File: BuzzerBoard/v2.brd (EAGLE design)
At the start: 48 x 15 mm, 10 parts, among them J1 p0, U1 LM386MX-1/NOPB

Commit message: starting on v2
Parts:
- removed R1: 23BR100KLFTR, BuzzerLib:SOT_23BR100KLFTR
- removed U$1: SMS-1308MS-2-R, BuzzerLib:SMS-1308MS-2-R
- added C5: GRM188R60J106ME47D, BuzzerLib:0603
- added C6: C2012X5R1A336M125AC, BuzzerLib:0805
- added J2: (no value), SparkFun-Connectors:1X02
- added U2: Value, BuzzerLib:DRC0010J
- added U3: LQM2HPN1R5MG0L, BuzzerLib:1008
- moved R2 19.7 mm to (34.1, 8.19), turned to 180 degrees
- moved C2 19.5 mm to (34.1, 11.7), turned to 270 degrees
- moved C4 17.0 mm to (38.9, 12.7)
- moved C3 11.0 mm to (43.4, 7.49)
- moved C1 11.0 mm to (38.9, 8.48)
- moved U1 11.0 mm to (38.9, 4.08)
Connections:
- removed net IN+: R1.2, U1.3
- new net 3V_REG: C6.1, U1.6, U2.1, U2.10
- new net N$6: U2.2, U3.2
- new net N$7: U2.4, U3.1
- net +: now also J2.1; no longer U$1.+
- net 3.3V: now also C5.1, U2.5, U2.6, U2.7, U2.8; no longer U1.6
- net GND: now also C5.2, C6.2, J2.2, U2.11, U2.3, U2.9; no longer R1.1, U$1.-
- net P0: now also U1.3; no longer R1.3
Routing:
- net GND: track 21.3 -> 0.00 mm, vias 9 -> 0
- net +: track 13.9 -> 0.00 mm
- net VOUT: track 32.7 -> 21.1 mm, vias 4 -> 0
- net P0: track 10.6 -> 0.00 mm
- net IN+: track 8.09 -> 0.00 mm
- net GAIN: track 4.61 -> 0.00 mm
- net BYPASS: track 4.51 -> 0.00 mm
- net N$2: track 4.42 -> 0.00 mm
- net N$1: track 1.92 -> 0.00 mm

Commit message: progress on the v2 board
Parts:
- removed U2: Value, BuzzerLib:DRC0010J
- removed U3: LQM2HPN1R5MG0L, BuzzerLib:1008
- added C7: 100nf, Seeed-Capacitor:C0603
- added J3: inv, SparkFun-Connectors:1X02
- C5: value GRM188R60J106ME47D -> 100pf; device BuzzerLib:0603 -> Seeed-Capacitor:C0603
- C6: value C2012X5R1A336M125AC -> 100nf; device BuzzerLib:0805 -> Seeed-Capacitor:C0603
- J1: value p0 -> input
- J2: value (none) -> speaker
- moved U$2 21.0 mm to (24.0, 3.00)
- moved R2 20.3 mm to (13.9, 9.47), turned to 270 degrees
- moved C2 20.2 mm to (13.9, 11.4), turned to 180 degrees
- moved J2 19.9 mm to (26.6, 10.7)
- moved C4 18.7 mm to (20.3, 11.7)
- moved U1 14.8 mm to (24.2, 3.38)
- moved C1 14.7 mm to (24.1, 7.28)
- moved C3 14.4 mm to (29.2, 4.84)
- moved C5 14.0 mm to (19.4, 5.50), turned to 180 degrees
- moved C6 6.39 mm to (15.7, 5.50), turned to 0 degrees
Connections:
- removed net 3V_REG: C6.1, U1.6, U2.1, U2.10
- removed net N$6: U2.2, U3.2
- removed net N$7: U2.4, U3.1
- new net IN-: J3.2, U1.2
- new net N$3: C5.1, J3.1
- net +: now also J2.2; no longer J2.1
- net 3.3V: now also C6.2, U1.6; no longer C5.1, U2.5, U2.6, U2.7, U2.8
- net GND: now also C6.1, C7.1, J2.1; no longer C6.2, J2.2, U1.2, U2.11, U2.3, U2.9
- net P0: now also C7.2
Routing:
- net VOUT: track 21.1 -> 0.00 mm
- net P0: track 0.00 -> 6.10 mm
- net IN-: track 0.00 -> 4.89 mm
- net N$3: track 0.00 -> 4.78 mm
- net +: track 0.00 -> 4.68 mm
- net GAIN: track 0.00 -> 3.41 mm
- net N$2: track 0.00 -> 3.33 mm
- net 3.3V: track 0.00 -> 3.20 mm
- net N$1: track 0.00 -> 1.99 mm
- added copper zone on layer 16, net 3.3V
- added copper zone on layer 1, net GND
- removed copper zone on layer 1, net 3.3V
- removed copper zone on layer 16, net GND
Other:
- board text added: "+"
- board text added: "3.3v"
- board text added: "GND"
- board text added: "Moto:Bit Speaker v1.0 32bits.io"
- board text added: "P0"
- board text added: "bee-boo-boop-beep"
- board text removed: "Moto:Bit Speaker v1.0 | 32bits.io"

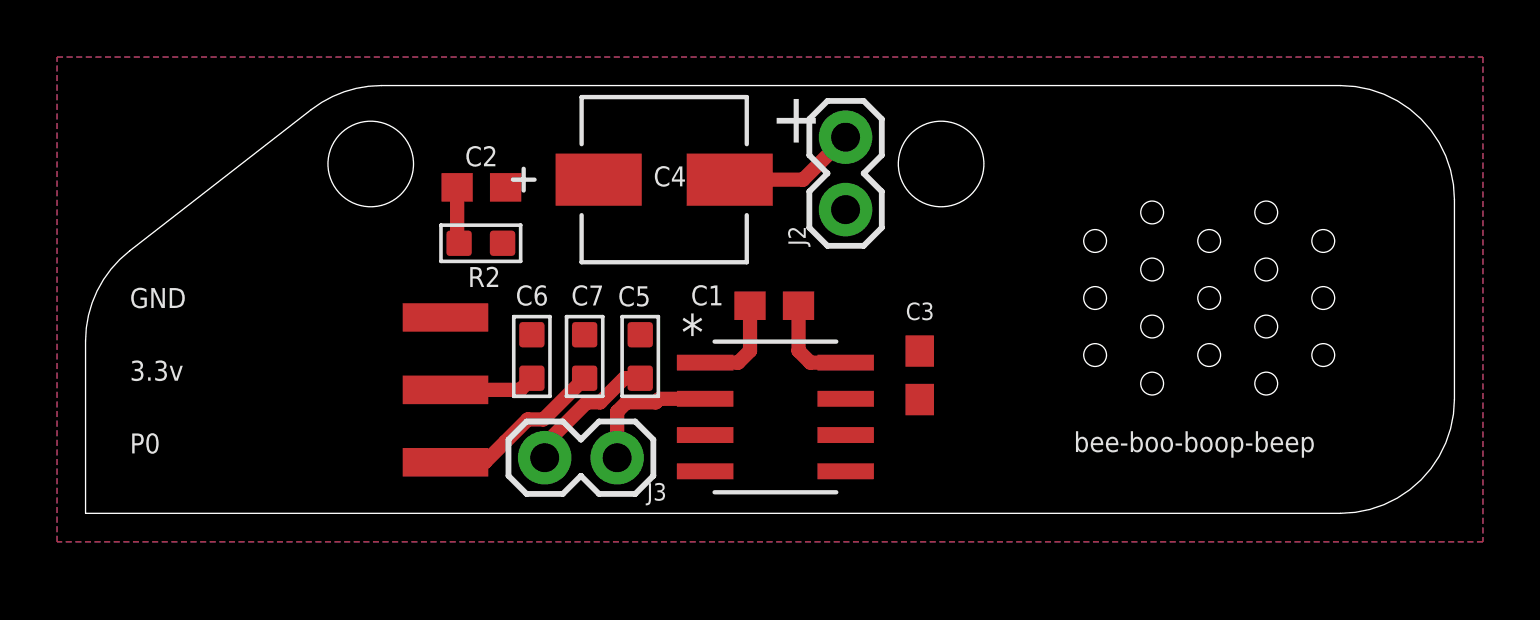
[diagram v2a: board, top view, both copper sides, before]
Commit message: Switching to LM48310 on the v2 board.
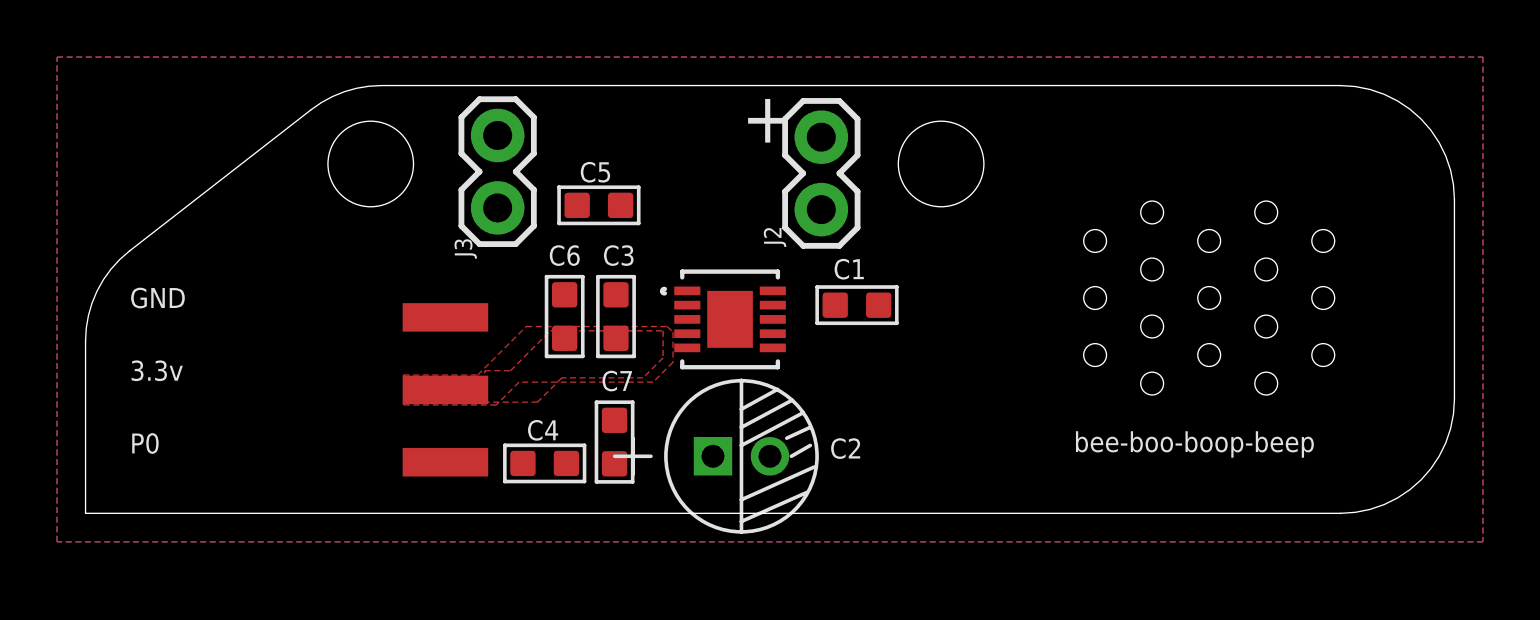
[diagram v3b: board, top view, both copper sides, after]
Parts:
- removed R2: 10R, Seeed-Resistor:R0603
- removed U1: LM386MX-1/NOPB, BuzzerLib:M08A
- added U2: LM48310SD/NOPBSDA10A-M, BuzzerLib:SDA10A-M
- C1: value 10uF -> 1uf; device SparkFun-Capacitors:0603 -> Seeed-Capacitor:C0603
- C2: value 47nF -> 10uf; device SparkFun-Capacitors:0603 -> Seeed-Capacitor:PC-D5.3MM
- C3: value 0.1uF -> 1uf; device SparkFun-Capacitors:0603 -> Seeed-Capacitor:C0603
- C4: value 6SVPE220MW -> 1uf; device BuzzerLib:PCAP_SVP_B6 -> Seeed-Capacitor:C0603
- C5: value 100pf -> 1uf
- moved C2 13.1 mm to (23.0, 2.00), turned to 0 degrees
- moved J3 11.4 mm to (14.4, 13.2), turned to 270 degrees
- moved C3 10.8 mm to (18.6, 6.90), turned to 0 degrees
- moved C4 10.8 mm to (16.1, 1.75), turned to 270 degrees
- moved C5 5.49 mm to (18.0, 10.8), turned to 270 degrees
- moved C7 3.18 mm to (18.6, 2.50)
- moved C1 2.90 mm to (27.1, 7.30), turned to 270 degrees
- moved C6 1.81 mm to (16.8, 6.90)
- moved J2 0.85 mm to (25.8, 10.7)
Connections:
- removed net BYPASS: C3.1, U1.7
- removed net GAIN: C1.2, U1.8
- removed net IN-: J3.2, U1.2
- removed net N$1: C2.2, R2.2
- removed net N$2: C1.1, U1.1
- removed net N$3: C5.1, J3.1
- removed net VOUT: C2.1, C4.1, U1.5
- new net -: J2.1, U2.7
- new net BAL_IN: C5.1, U2.1
- new net BAL_IN_RAW: C5.2, J3.2
- new net P0_RAW: C4.2, J1.3
- net +: now also U2.10; no longer C4.2
- net 3.3V: now also C1.2, C2.+, C3.2, U2.3, U2.4, U2.5, U2.9; no longer U1.6
- net GND: now also C1.1, C2.-, C3.1, J3.1, U2.11, U2.8; no longer C3.2, C5.2, J2.1, R2.1, U1.4
- net P0: now also C4.1, U2.2; no longer J1.3, U1.3
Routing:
- net P0: track 6.10 -> 0.00 mm
- net IN-: track 4.89 -> 0.00 mm
- net N$3: track 4.78 -> 0.00 mm
- net +: track 4.68 -> 0.00 mm
- net GAIN: track 3.41 -> 0.00 mm
- net N$2: track 3.33 -> 0.00 mm
- net 3.3V: track 3.20 -> 0.00 mm
- net N$1: track 1.99 -> 0.00 mm
- added copper zone on layer 1, net 3.3V
- added copper zone on layer 1, net N$1
